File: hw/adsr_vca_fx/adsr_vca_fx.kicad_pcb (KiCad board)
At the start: 4 copper layers, 88.9 x 91.4 mm, 116 parts, among them J1 Conn_01x03, J10 VCA2 Extern, J11 Conn_01x04, J12 Conn_01x03, J2 Conn_02x02_Odd_Even, J3 Conn_02x02_Odd_Even, J4 Audio Input, J5 Audio Output, J6 Conn_02x05_Odd_Even, J7 Envelope2 Extern, J8 Envelope1 Extern, J9 VCA1 Extern, Q1 HX2301A PMOS, SW1 SW_Push, SW2 SW_Push, SW3 SW_Push, SW4 SW_Push, U1 TL972, U10 TPS60403, U2 MCP603-xCH, U3 STM32L432KBUx, U4 LM13700, U5 TL972, U6 TPS563200, U7 SE8233X2, U8 TPS60403, U9 TPS60403

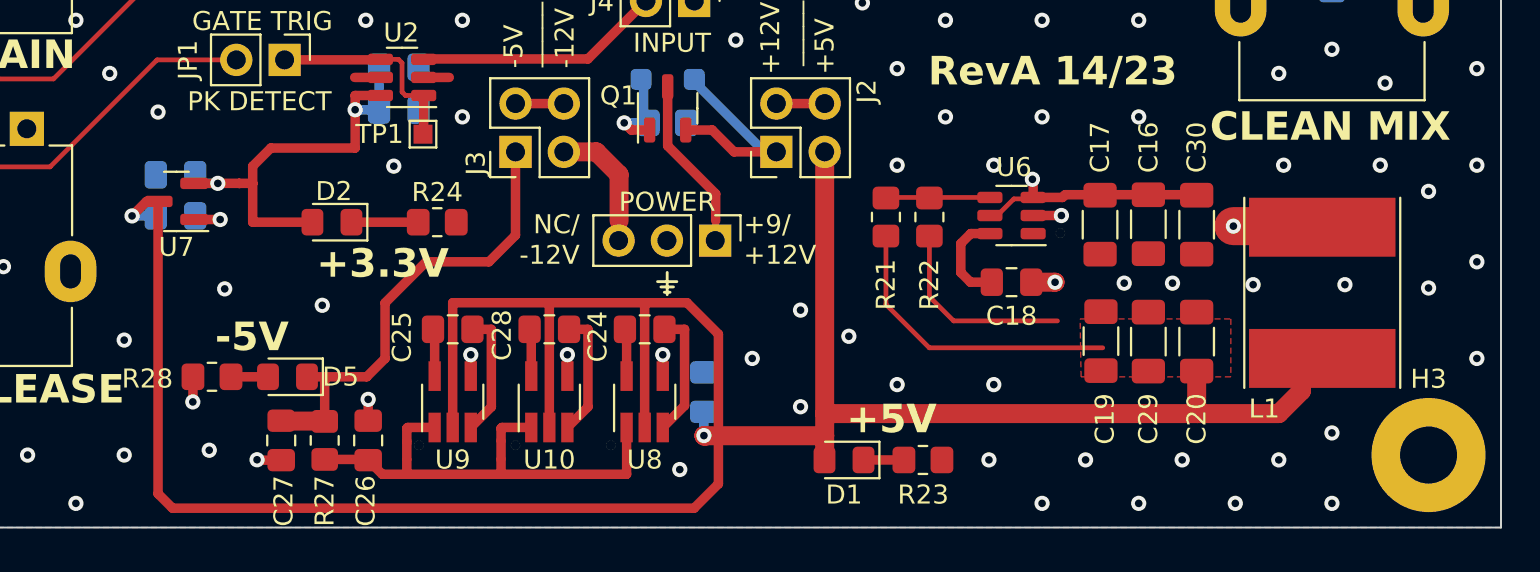
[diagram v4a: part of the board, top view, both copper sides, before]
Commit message: RevB; simplified power supply
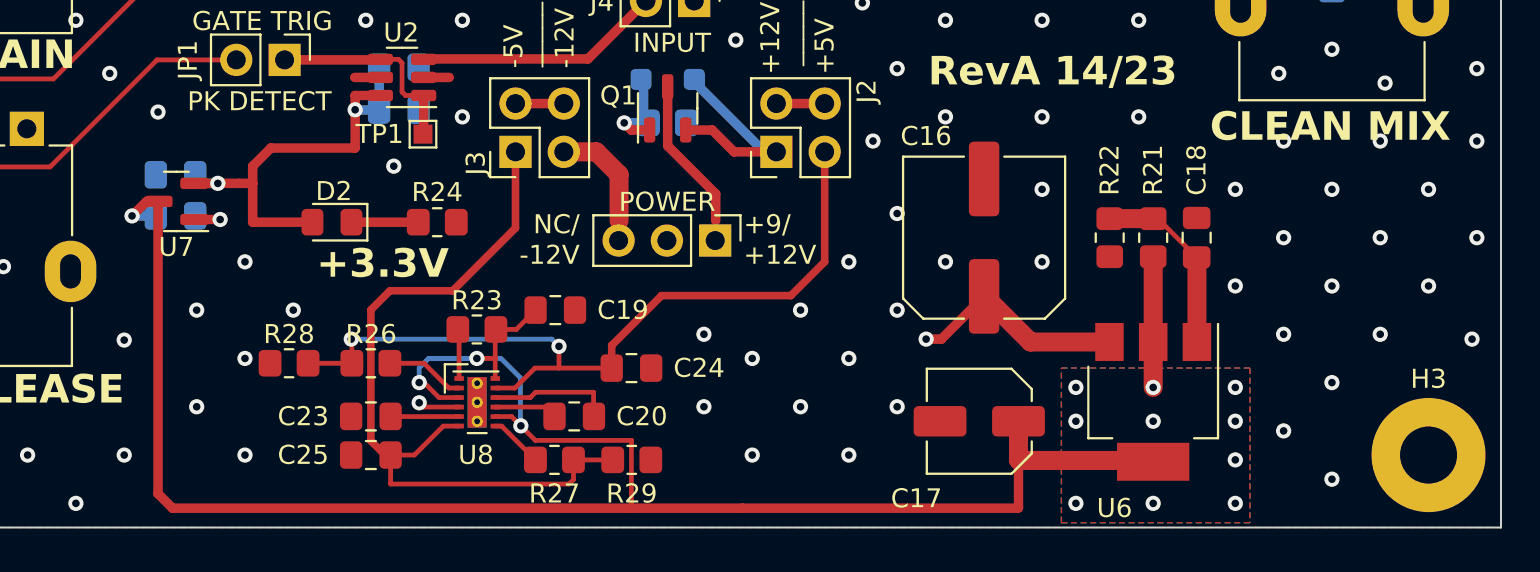
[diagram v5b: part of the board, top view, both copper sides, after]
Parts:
- removed C26: 2.2uF, Capacitor_SMD:C_0805_2012Metric_Pad1.18x1.45mm_HandSolder
- removed C27: 100nF, Capacitor_SMD:C_0805_2012Metric_Pad1.18x1.45mm_HandSolder
- removed C28: 1uf, Capacitor_SMD:C_0805_2012Metric_Pad1.18x1.45mm_HandSolder
- removed C29: 22uF, Resistor_SMD:R_1206_3216Metric_Pad1.30x1.75mm_HandSolder
- removed C30: 100nF, Resistor_SMD:R_1206_3216Metric_Pad1.30x1.75mm_HandSolder
- removed D1, D5: RED, LED_SMD:LED_0805_2012Metric_Pad1.15x1.40mm_HandSolder
- removed L1: 4.7uH, Inductor_SMD:L_Taiyo-Yuden_NR-80xx_HandSoldering
- removed NT1, NT2: NetTie_2, NetTie:NetTie-2_SMD_Pad0.5mm
- removed U10, U9: TPS60403, Package_TO_SOT_SMD:SOT-23-5_HandSoldering
- added R26: 470R, Resistor_SMD:R_0805_2012Metric_Pad1.20x1.40mm_HandSolder, F.Cu at (105.7, 133.6)
- added R29: 150R, Resistor_SMD:R_0805_2012Metric_Pad1.20x1.40mm_HandSolder, F.Cu at (119.4, 138.7)
- C16: value 10uF -> 100u; footprint Resistor_SMD:R_1206_3216Metric_Pad1.30x1.75mm_HandSolder -> Capacitor_SMD:C_Elec_8x5.4
- C17: value 10uF -> 20u; footprint Resistor_SMD:R_1206_3216Metric_Pad1.30x1.75mm_HandSolder -> Capacitor_SMD:C_Elec_5x5.4
- C18: value 100nF -> 5.6n
- C19: value 22uF -> 4.7u; footprint Resistor_SMD:R_1206_3216Metric_Pad1.30x1.75mm_HandSolder -> Capacitor_SMD:C_0805_2012Metric_Pad1.18x1.45mm_HandSolder
- C20: value 22uF -> 1u; footprint Resistor_SMD:R_1206_3216Metric_Pad1.30x1.75mm_HandSolder -> Capacitor_SMD:C_0805_2012Metric_Pad1.18x1.45mm_HandSolder
- C23: value 1uf -> 10u; moved to F.Cu
- C24, C25: value 1uf -> 2.2u
- R21: value 56K -> 300R
- R22: value 10K -> 1K
- R23: value 2K2 -> 10K
- R27: value 47R -> 470R
- R28: value 2K2 -> 150
- U6: value TPS563200 -> LM1117MP-ADJ; footprint Package_TO_SOT_SMD:SOT-23-6 -> Package_TO_SOT_SMD:SOT-223-3_TabPin2
- U8: value TPS60403 -> LM27762; footprint Package_TO_SOT_SMD:SOT-23-5_HandSoldering -> Package_SON:WSON-12-1EP_3x2mm_P0.5mm_EP1x2.65_ThermalVias
- moved C20 33.0 mm to (116.4, 136.4), turned to 0 degrees
- moved C19 28.7 mm to (115.4, 130.8), turned to 0 degrees
- moved R23 24.4 mm to (111.3, 131.8), turned to 180 degrees
- moved C23 17.6 mm to (105.7, 136.4), turned to 180 degrees
- moved R21 14.1 mm to (146.8, 127.0)
- moved U6 12.3 mm to (146.8, 135.6), turned to -90 degrees
- moved C17 12.1 mm to (137.7, 136.7), turned to 180 degrees
- moved R27 12.1 mm to (115.3, 138.7), turned to 0 degrees
- moved C18 10.0 mm to (149.1, 127.0), turned to 90 degrees
- moved R22 9.54 mm to (144.5, 127.0)
- moved U8 8.81 mm to (111.3, 135.7), turned to 0 degrees
- moved C16 8.66 mm to (137.9, 127.0), turned to 90 degrees
- moved C25 7.89 mm to (105.7, 138.4)
- moved R28 4.12 mm to (101.4, 133.6)
- moved C24 2.15 mm to (119.4, 133.9), turned to 0 degrees
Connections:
- C17 pad 1: /PowerSupply/PolarityProtection/VOUT -> /PowerSupply/+5V
- C18 pad 1: Net-(U6-VBST) -> Net-(U6-ADJ)
- C18 pad 2: Net-(U6-SW) -> GND
- C20 pad 1: /PowerSupply/+5V -> Net-(U8-C-)
- C20 pad 2: GND -> Net-(U8-C+)
- C23 pad 1: /PowerSupply/+5V -> Net-(U8-CP)
- C24 pad 1: Net-(U8-CFLY-) -> /PowerSupply/Dual Rail Regulated Charge Pump/CP_VOUT_POS
- C24 pad 2: Net-(U8-CFLY+) -> GND
- C25 pad 1: Net-(U9-CFLY-) -> /PowerSupply/-5V
- C25 pad 2: Net-(U9-CFLY+) -> GND
- J2 pad 3: /PowerSupply/+5V -> /PowerSupply/Dual Rail Regulated Charge Pump/CP_VOUT_POS
- R21 pad 2: Net-(U6-VFB) -> Net-(U6-ADJ)
- R22 pad 1: Net-(U6-VFB) -> Net-(U6-ADJ)
- R23 pad 1: Net-(D1-K) -> /PowerSupply/+5V
- R23 pad 2: GND -> Net-(U8-PGOOD)
- R27 pad 1: Net-(U8-OUT) -> Net-(U8-FB-)
- R28 pad 1: Net-(D5-A) -> /PowerSupply/Dual Rail Regulated Charge Pump/CP_VOUT_POS
- U6 pad 1: GND -> Net-(U6-ADJ)
- U6 pad 2: Net-(U6-SW) -> /PowerSupply/+5V
- U8 pad 1: Net-(U8-OUT) -> Net-(U8-PGOOD)
- U8 pad 2: /PowerSupply/+5V -> Net-(U8-FB+)
- U8 pad 3: Net-(U8-CFLY-) -> /PowerSupply/+5V
- U8 pad 5: Net-(U8-CFLY+) -> Net-(U8-CP)
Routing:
- net /PowerSupply/+5V: track 161.3 -> 113.5 mm, vias 2 -> 14
- net /PowerSupply/Dual Rail Regulated Charge Pump/CP_VOUT_POS: track 0.00 -> 42.3 mm, vias 0 -> 2
- net Net-(U6-SW): track 20.4 -> 0.00 mm, vias 3 -> 0
- net Net-(U8-OUT): track 20.2 -> 0.00 mm
- net /PowerSupply/-5V: track 24.8 -> 40.4 mm
- net GND: track 24.8 -> 9.46 mm, vias 180 -> 183
- net Net-(U6-ADJ): track 0.00 -> 9.87 mm
- net Net-(U8-CFLY-): track 6.70 -> 0.00 mm
- net Net-(U9-CFLY-): track 6.60 -> 0.00 mm
- net Net-(U10-CFLY-): track 6.60 -> 0.00 mm
- net Net-(U8-C+): track 0.00 -> 6.53 mm
- net Net-(U6-VFB): track 5.70 -> 0.00 mm
- net Net-(U6-VBST): track 5.11 -> 0.00 mm
- net Net-(U8-FB+): track 0.00 -> 4.18 mm
- net Net-(U8-CP): track 0.00 -> 3.60 mm
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- added copper zone on B.Cu, net /PowerSupply/+5V
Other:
- board text removed: "+5V"
- board text removed: "-5V"
